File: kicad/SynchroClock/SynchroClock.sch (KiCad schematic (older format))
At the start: 13 parts

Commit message: using atmega328 for now
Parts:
- removed IC?: ATTINY85-P, DIP8, symbol ATTINY85-P
- added D? (x2): 1N4001, pth-semi:DO-41, symbol 1N4001
- added P?: CONN_01X02, symbol CONN_01X02
- added U?: ATMEGA328-PU, dip-sip:DIP-28, symbol ATMEGA328-PU
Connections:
- net labels removed: A, B, CLOCK_A, CLOCK_B, SCL, SDA, SQW
- wire segments 34 -> 46
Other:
- moved on the sheet: D?, U?
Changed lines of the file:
@@
-$EndComp
-$Comp
-L ATTINY85-P IC?
-U 1 1 58C75634
-P 8200 3450
-F 0 "IC?" H 7050 3850 50  0000 C CNN
-F 1 "ATTINY85-P" H 9200 3050 50  0000 C CNN
-F 2 "DIP8" H 9200 3450 50  0000 C CIN
-F 3 "" H 8200 3450 50  0000 C CNN
-	1    8200 3450
-	1    0    0    -1
 $EndComp
 $Comp
 L DS3231 U?
 U 1 1 58C756EE
-P 5400 3400
-F 0 "U?" H 5300 3875 50  0000 R CNN
-F 1 "DS3231" H 5300 3800 50  0000 R CNN
-F 2 "Housings_SOIC:SOIC-16_7.5x10.3mm_Pitch1.27mm" H 5450 3000 50  0001 L CNN
-F 3 "" H 5670 3650 50  0001 C CNN
-	1    5400 3400
-	1    0    0    -1
-$EndComp
-Text Label 4700 3300 0    60   ~ 0
-SCL
-Text Label 3950 3350 2    60   ~ 0
-SCL
-Text Label 3950 3450 2    60   ~ 0
-SDA
-Text Label 4700 3400 0    60   ~ 0
-SDA
-Text Label 6650 3400 0    60   ~ 0
-SCL
-Text Label 6650 3200 0    60   ~ 0
-SDA
-Wire Wire Line
-	4900 3300 4700 3300
-Wire Wire Line
-	4900 3400 4700 3400
-Wire Wire Line
-	3750 3350 3950 3350
-Wire Wire Line
-	3750 3450 3950 3450
-Wire Wire Line
-	6850 3200 6650 3200
-Wire Wire Line
-	6850 3400 6650 3400
+P 4250 2400
+F 0 "U?" H 4150 2875 50  0000 R CNN
+F 1 "DS3231" H 4150 2800 50  0000 R CNN
+F 2 "Housings_SOIC:SOIC-16_7.5x10.3mm_Pitch1.27mm" H 4300 2000 50  0001 L CNN
+F 3 "" H 4520 2650 50  0001 C CNN
+	1    4250 2400
+	0    -1   -1   0
+$EndComp
 $Comp
 L 2N3904 Q?
@@
 Connection ~ 2300 5900
 Wire Wire Line
-	2300 5900 3250 5900
-Wire Wire Line
 	4750 5200 4750 5500
 Wire Wire Line
@@
 	1500 6200 1700 6200
 Connection ~ 1500 5900
-Text Label 5600 5900 0    60   ~ 0
-A
-Text Label 1400 5900 2    60   ~ 0
-B
-Wire Wire Line
-	5600 5900 5500 5900
-Wire Wire Line
-	1400 5900 1500 5900
-Wire Wire Line
-	3650 5900 4750 5900
 $Comp
 L +3.3 #PWR?
@@
 L 1N4001 D?
 U 1 1 58D095EF
-P 3450 6050
-F 0 "D?" V 3600 6050 50  0000 C CNN
-F 1 "1N4001" V 3700 6000 50  0000 C CNN
-F 2 "pth-semi:DO-41" H 3450 5900 50  0001 C CNN
-F 3 "" H 3450 6050 60  0000 C CNN
-F 4 "DIODE 1N4001" H 3450 5800 60  0001 C CNN "BOM"
-	1    3450 6050
+P 3800 6050
+F 0 "D?" V 3950 6050 50  0000 C CNN
+F 1 "1N4001" V 4050 6000 50  0000 C CNN
+F 2 "pth-semi:DO-41" H 3800 5900 50  0001 C CNN
+F 3 "" H 3800 6050 60  0000 C CNN
+F 4 "DIODE 1N4001" H 3800 5800 60  0001 C CNN "BOM"
+	1    3800 6050
 	0    -1   1    0
 $EndComp
@@
 L 1N4001 D?
 U 1 1 58D0972D
-P 3450 5750
-F 0 "D?" V 3600 5750 50  0000 C CNN
-F 1 "1N4001" V 3700 5700 50  0000 C CNN
-F 2 "pth-semi:DO-41" H 3450 5600 50  0001 C CNN
-F 3 "" H 3450 5750 60  0000 C CNN
-F 4 "DIODE 1N4001" H 3450 5500 60  0001 C CNN "BOM"
-	1    3450 5750
+P 3800 5750
+F 0 "D?" V 3950 5750 50  0000 C CNN
+F 1 "1N4001" V 4050 5700 50  0000 C CNN
+F 2 "pth-semi:DO-41" H 3800 5600 50  0001 C CNN
+F 3 "" H 3800 5750 60  0000 C CNN
+F 4 "DIODE 1N4001" H 3800 5500 60  0001 C CNN "BOM"
+	1    3800 5750
 	0    1    -1   0
 $EndComp
-Wire Wire Line
-	3350 5750 3250 5750
-Wire Wire Line
-	3250 5750 3250 6450
-Wire Wire Line
-	3250 6050 3350 6050
-Wire Wire Line
-	3550 5750 3650 5750
-Wire Wire Line
-	3650 5750 3650 6450
-Wire Wire Line
-	3650 6050 3550 6050
-Connection ~ 3650 5900
-Connection ~ 3250 5900
-Connection ~ 3250 6050
-Connection ~ 3650 6050
-Text Label 3250 6450 3    60   ~ 0
-CLOCK_B
-Text Label 3650 6450 3    60   ~ 0
-CLOCK_A
-Text Label 6100 3300 2    60   ~ 0
-SQW
-Wire Wire Line
-	5900 3300 6100 3300
-Text Label 1700 3550 0    60   ~ 0
-SQW
-Wire Wire Line
-	1950 3550 1700 3550
+$Comp
+L 1N4001 D?
+U 1 1 58D3369C
+P 2950 5750
+F 0 "D?" V 3100 5750 50  0000 C CNN
+F 1 "1N4001" V 3200 5700 50  0000 C CNN
+F 2 "pth-semi:DO-41" H 2950 5600 50  0001 C CNN
+F 3 "" H 2950 5750 60  0000 C CNN
+F 4 "DIODE 1N4001" H 2950 5500 60  0001 C CNN "BOM"
+	1    2950 5750
+	0    1    -1   0
+$EndComp
+$Comp
+L 1N4001 D?
+U 1 1 58D336DD
+P 2950 6050
+F 0 "D?" V 3100 6050 50  0000 C CNN
+F 1 "1N4001" V 3200 6000 50  0000 C CNN
+F 2 "pth-semi:DO-41" H 2950 5900 50  0001 C CNN
+F 3 "" H 2950 6050 60  0000 C CNN
+F 4 "DIODE 1N4001" H 2950 5800 60  0001 C CNN "BOM"
+	1    2950 6050
+	0    -1   1    0
+$EndComp
+Wire Wire Line
+	2850 5750 2850 6050
+Wire Wire Line
+	3050 5750 3050 6050
+Wire Wire Line
+	3700 5750 3700 6050
+Wire Wire Line
+	3900 5750 3900 6050
+Connection ~ 3900 5900
+Connection ~ 3700 5900
+Connection ~ 3050 5900
+Connection ~ 2850 5900
+Wire Wire Line
+	4750 5900 3900 5900
+Wire Wire Line
+	2850 5900 2300 5900
+$Comp
+L CONN_01X02 P?
+U 1 1 58D33A1E
+P 3350 6750
+F 0 "P?" H 3350 6900 50  0000 C CNN
+F 1 "CONN_01X02" V 3450 6750 50  0001 C CNN
+F 2 "" H 3350 6750 50  0000 C CNN
+F 3 "" H 3350 6750 50  0000 C CNN
+	1    3350 6750
+	0    1    1    0
+$EndComp
+Wire Wire Line
+	3050 5900 3300 5900
+Wire Wire Line
+	3300 5900 3300 6550
+Wire Wire Line
+	3400 6550 3400 5900
+Wire Wire Line
+	3400 5900 3700 5900
+$Comp
+L ATMEGA328-PU U?
+U 1 1 58D33C8A
+P 7500 3450
+F 0 "U?" H 7500 5000 50  0000 C CNN
+F 1 "ATMEGA328-PU" H 7500 4900 50  0000 C CNN
+F 2 "dip-sip:DIP-28" H 7500 2150 50  0001 C CNN
+F 3 "http://www.atmel.com/images/Atmel-8271-8-bit-AVR-Microcontroller-ATmega48A-48PA-88A-88PA-168A-168PA-328-328P_datasheet_Complete.pdf" H 7500 2050 50  0001 C CNN
+F 4 "ATMEGA328-PU" H 7500 1750 50  0001 C CNN "MPN"
+F 5 "Microchip" H 7500 1850 50  0001 C CNN "Manuf"
+F 6 "Microchip ATMEGA328-PU" H 7500 1950 50  0001 C CNN "BOM"
+	1    7500 3450
+	-1   0    0    -1
+$EndComp
+Wire Wire Line
+	3750 3350 4150 3350
+Wire Wire Line
+	4150 2900 4150 3550
+Wire Wire Line
+	4250 2900 4250 3450
+Wire Wire Line
+	3750 3450 6650 3450
+Connection ~ 4250 3450
+Wire Wire Line
+	4150 3550 6650 3550
+Connection ~ 4150 3350
+Wire Wire Line
+	4150 1900 1800 1900
+Wire Wire Line
+	1800 1900 1800 3550
+Wire Wire Line
+	1800 3550 1950 3550
+Wire Wire Line
+	6650 4350 6100 4350
+Wire Wire Line
+	6100 4350 6100 5900
+Wire Wire Line
+	6100 5900 5500 5900
+Wire Wire Line
+	6650 4250 6000 4250
+Wire Wire Line
+	6000 4250 6000 4900
+Wire Wire Line
+	6000 4900 1300 4900
+Wire Wire Line
+	1300 4900 1300 5900
+Wire Wire Line
+	1300 5900 1500 5900
+Wire Wire Line
+	4150 1900 4150 1700
+Wire Wire Line
+	4150 1700 6300 1700
+Wire Wire Line
+	6300 1700 6300 4150
+Wire Wire Line
+	6300 4150 6650 4150
 $EndSCHEMATC

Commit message: update schematic (WIP)
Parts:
- removed D? (x4): 1N4001, pth-semi:DO-41, symbol 1N4001
- removed P?: CONN_01X02, symbol CONN_01X02
- removed Q? (x2): 2N3904, pth-semi:TO-92, symbol 2N3904
- removed Q? (x2): 2N3906, pth-semi:TO-92, symbol 2N3906
- removed R? (x4): 2.2k, symbol R
- added U?: DRV8838, symbol DRV8838
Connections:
- net labels added: 1HZ, ENABLE, PHASE, SCL, SDA
- wire segments 46 -> 33
- no-connect marks 0 -> 29
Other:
- moved on the sheet: U?

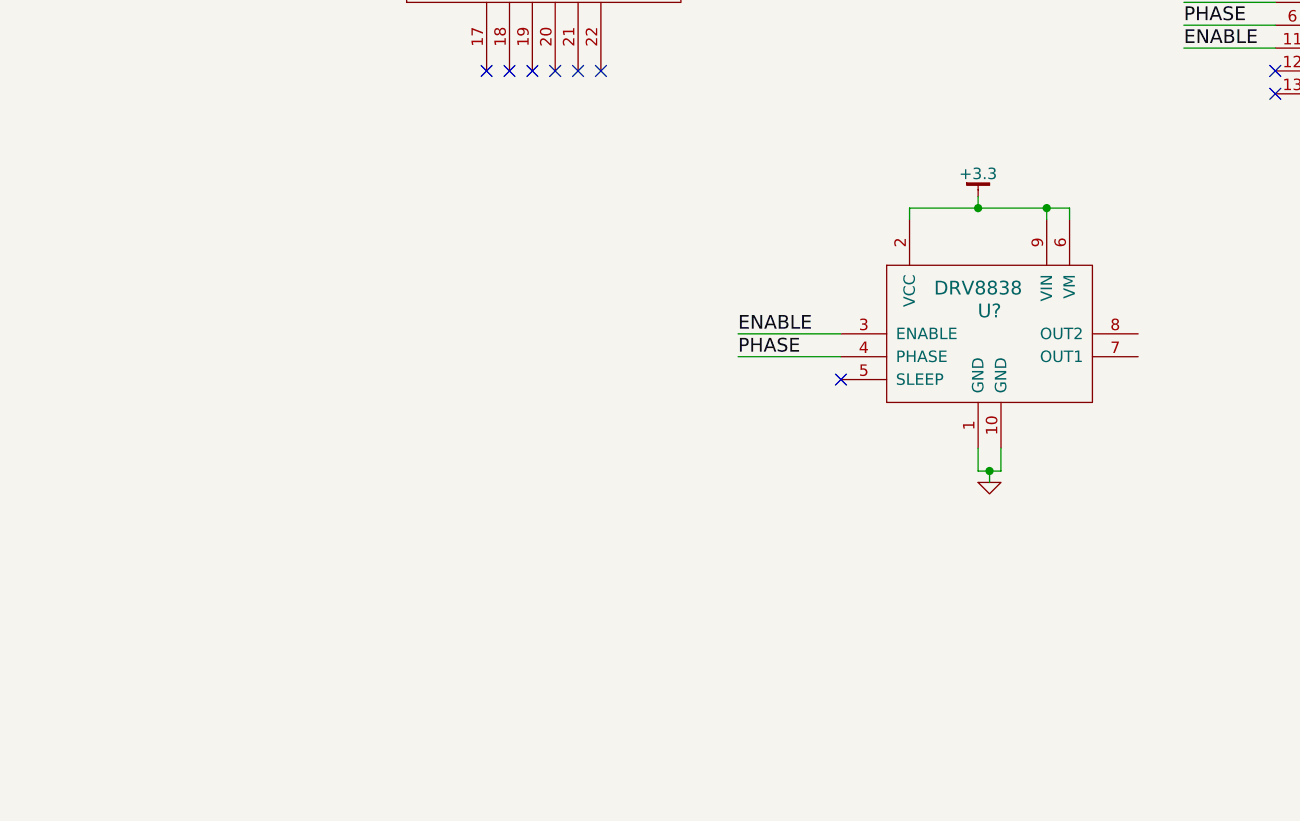
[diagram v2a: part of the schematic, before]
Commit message: added diodes to drop clock output voltage
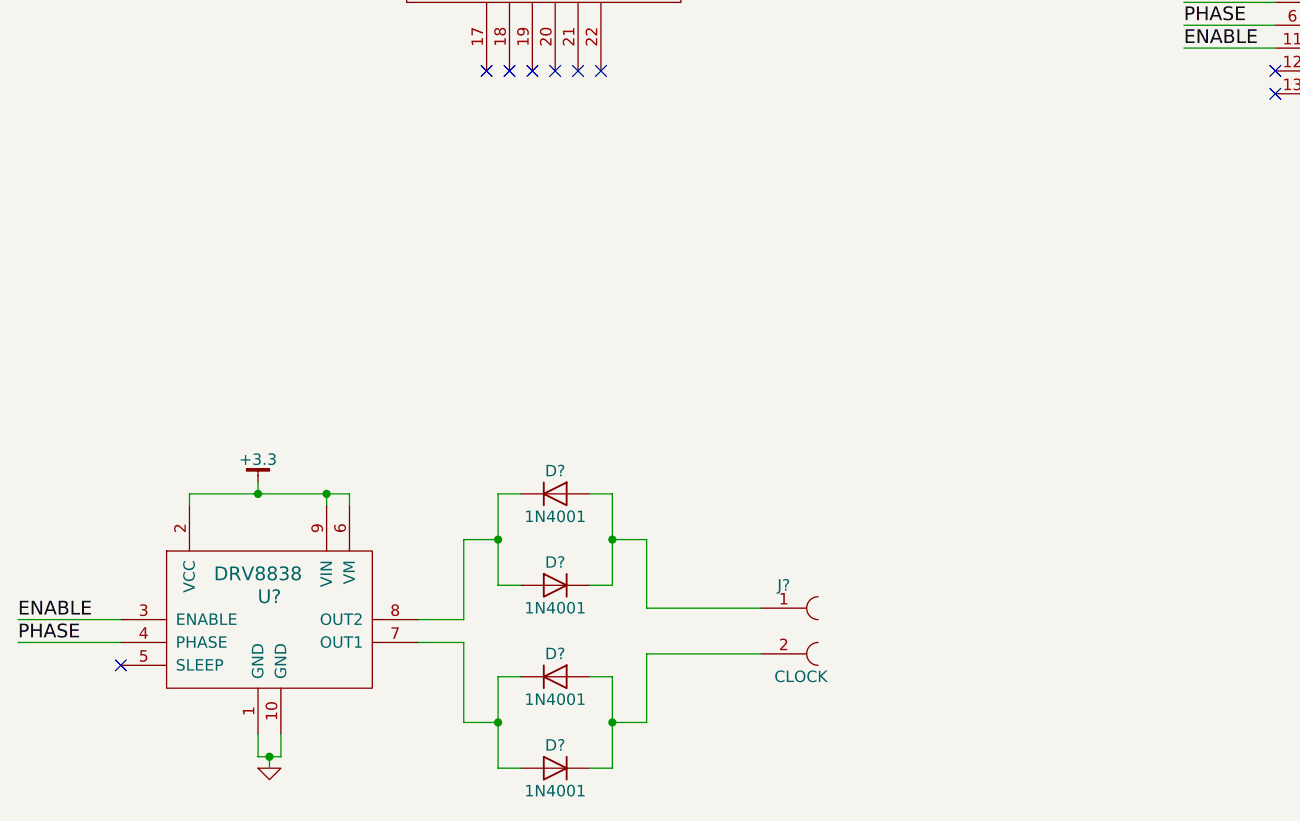
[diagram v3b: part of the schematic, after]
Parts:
- added D? (x4): 1N4001, Diodes_THT:D_DO-41_SOD81_Horizontal_RM10, symbol 1N4001
- added J?: CLOCK, symbol CONN_01X02_FEMALE
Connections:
- net at U?.7 (OUT1): now also D?.1 (K), D?.2 (A)
- net at U?.8 (OUT2): now also D?.1 (K), D?.2 (A)
- new net: D?.1 (K), D?.2 (A), J?.1
- new net: D?.1 (K), D?.2 (A), J?.2
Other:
- moved on the sheet: U?
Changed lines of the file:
@@
 Wire Wire Line
 	4800 3550 5100 3550
-Text Label 4750 5700 0    60   ~ 0
+Text Label 1600 6950 0    60   ~ 0
 ENABLE
-Text Label 4750 5800 0    60   ~ 0
+Text Label 1600 7050 0    60   ~ 0
 PHASE
 Wire Wire Line
-	4750 5700 5200 5700
+	1600 6950 2050 6950
 Wire Wire Line
-	4750 5800 5200 5800
+	1600 7050 2050 7050
 $Comp
 L DRV8838 U?
 U 1 1 58D7D0C2
-P 5850 5400
-F 0 "U?" H 5850 5200 60  0000 C CNN
-F 1 "DRV8838" H 5800 5300 60  0000 C CNN
-F 2 "" H 5850 5400 60  0001 C CNN
-F 3 "" H 5850 5400 60  0001 C CNN
-	1    5850 5400
+P 2700 6650
+F 0 "U?" H 2700 6450 60  0000 C CNN
+F 1 "DRV8838" H 2650 6550 60  0000 C CNN
+F 2 "" H 2700 6650 60  0001 C CNN
+F 3 "" H 2700 6650 60  0001 C CNN
+	1    2700 6650
 	1    0    0    -1
 $EndComp
-NoConn ~ 5200 5900
+NoConn ~ 2050 7150
 $Comp
 L GND #PWR?
 U 1 1 58D7D0FF
-P 5850 6350
-F 0 "#PWR?" H 5850 6350 30  0001 C CNN
-F 1 "GND" H 5850 6280 30  0001 C CNN
-F 2 "" H 5850 6350 60  0000 C CNN
-F 3 "" H 5850 6350 60  0000 C CNN
-	1    5850 6350
+P 2700 7600
+F 0 "#PWR?" H 2700 7600 30  0001 C CNN
+F 1 "GND" H 2700 7530 30  0001 C CNN
+F 2 "" H 2700 7600 60  0000 C CNN
+F 3 "" H 2700 7600 60  0000 C CNN
+	1    2700 7600
 	1    0    0    -1
 $EndComp
 Wire Wire Line
-	5850 6350 5850 6300
+	2700 7600 2700 7550
 Wire Wire Line
-	5800 6300 5900 6300
+	2650 7550 2750 7550
 Wire Wire Line
-	5900 6300 5900 6200
+	2750 7550 2750 7450
 Wire Wire Line
-	5800 6200 5800 6300
-Connection ~ 5850 6300
+	2650 7450 2650 7550
+Connection ~ 2700 7550
 $Comp
 L +3.3 #PWR?
 U 1 1 58D7D184
-P 5800 5100
-F 0 "#PWR?" H 5800 5150 30  0001 C CNN
-F 1 "+3.3" H 5800 5200 50  0000 C CNN
-F 2 "" H 5800 5100 60  0000 C CNN
-F 3 "" H 5800 5100 60  0000 C CNN
-	1    5800 5100
+P 2650 6350
+F 0 "#PWR?" H 2650 6400 30  0001 C CNN
+F 1 "+3.3" H 2650 6450 50  0000 C CNN
+F 2 "" H 2650 6350 60  0000 C CNN
+F 3 "" H 2650 6350 60  0000 C CNN
+	1    2650 6350
 	1    0    0    -1
 $EndComp
 Wire Wire Line
-	5800 5100 5800 5150
+	2650 6350 2650 6400
 Wire Wire Line
-	5500 5200 5500 5150
+	2350 6450 2350 6400
 Wire Wire Line
-	5500 5150 6200 5150
+	2350 6400 3050 6400
 Wire Wire Line
-	6100 5150 6100 5200
+	2950 6400 2950 6450
 Wire Wire Line
-	6200 5150 6200 5200
-Connection ~ 5800 5150
-Connection ~ 6100 5150
+	3050 6400 3050 6450
+Connection ~ 2650 6400
+Connection ~ 2950 6400
+$Comp
+L 1N4001 D?
+U 1 1 58D7DA00
+P 3950 6400
+F 0 "D?" H 3950 6500 50  0000 C CNN
+F 1 "1N4001" H 3950 6300 50  0000 C CNN
+F 2 "Diodes_THT:D_DO-41_SOD81_Horizontal_RM10" H 3950 6225 50  0001 C CNN
+F 3 "" H 3950 6400 50  0001 C CNN
+	1    3950 6400
+	1    0    0    -1
+$EndComp
+$Comp
+L 1N4001 D?
+U 1 1 58D7DA54
+P 3950 6800
+F 0 "D?" H 3950 6900 50  0000 C CNN
+F 1 "1N4001" H 3950 6700 50  0000 C CNN
+F 2 "Diodes_THT:D_DO-41_SOD81_Horizontal_RM10" H 3950 6625 50  0001 C CNN
+F 3 "" H 3950 6800 50  0001 C CNN
+	1    3950 6800
+	-1   0    0    -1
+$EndComp
+$Comp
+L 1N4001 D?
+U 1 1 58D7DA9D
+P 3950 7200
+F 0 "D?" H 3950 7300 50  0000 C CNN
+F 1 "1N4001" H 3950 7100 50  0000 C CNN
+F 2 "Diodes_THT:D_DO-41_SOD81_Horizontal_RM10" H 3950 7025 50  0001 C CNN
+F 3 "" H 3950 7200 50  0001 C CNN
+	1    3950 7200
+	1    0    0    -1
+$EndComp
+$Comp
+L 1N4001 D?
+U 1 1 58D7DACD
+P 3950 7600
+F 0 "D?" H 3950 7700 50  0000 C CNN
+F 1 "1N4001" H 3950 7500 50  0000 C CNN
+F 2 "Diodes_THT:D_DO-41_SOD81_Horizontal_RM10" H 3950 7425 50  0001 C CNN
+F 3 "" H 3950 7600 50  0001 C CNN
+	1    3950 7600
+	-1   0    0    -1
+$EndComp
+Wire Wire Line
+	4100 7200 4200 7200
+Wire Wire Line
+	4200 7200 4200 7600
+Wire Wire Line
+	4200 7600 4100 7600
+Wire Wire Line
+	3800 7200 3700 7200
+Wire Wire Line
+	3700 7200 3700 7600
+Wire Wire Line
+	3700 7600 3800 7600
+Wire Wire Line
+	3350 7050 3550 7050
+Wire Wire Line
+	3550 7050 3550 7400
+Wire Wire Line
+	3550 7400 3700 7400
+Connection ~ 3700 7400
+$Comp
+L CONN_01X02_FEMALE J?
+U 1 1 58D7DDE0
+P 4950 7000
+F 0 "J?" H 4950 7200 50  0000 C CNN
+F 1 "CLOCK" H 5025 6800 50  0000 C CNN
+F 2 "" H 4950 7100 50  0001 C CNN
+F 3 "" H 4950 7100 50  0001 C CNN
+	1    4950 7000
+	1    0    0    -1
+$EndComp
+Wire Wire Line
+	3800 6400 3700 6400
+Wire Wire Line
+	3700 6400 3700 6800
+Wire Wire Line
+	3700 6800 3800 6800
+Wire Wire Line
+	3350 6950 3550 6950
+Wire Wire Line
+	3550 6950 3550 6600
+Wire Wire Line
+	3550 6600 3700 6600
+Connection ~ 3700 6600
+Wire Wire Line
+	4100 6400 4200 6400
+Wire Wire Line
+	4200 6400 4200 6800
+Wire Wire Line
+	4200 6800 4100 6800
+Wire Wire Line
+	4850 6900 4350 6900
+Wire Wire Line
+	4350 6900 4350 6600
+Wire Wire Line
+	4350 6600 4200 6600
+Connection ~ 4200 6600
+Wire Wire Line
+	4850 7100 4350 7100
+Wire Wire Line
+	4350 7100 4350 7400
+Wire Wire Line
+	4350 7400 4200 7400
+Connection ~ 4200 7400
 $EndSCHEMATC

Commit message: more schematic work
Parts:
- added D1: LED, LEDs:LED_D3.0mm, symbol LED
- added R1, R2, R3, R7, R8, R9: 10k, Resistors_THT:R_Axial_DIN0204_L3.6mm_D1.6mm_P1.90mm_Vertical, symbol R
- added R4, R5: 1k, Resistors_THT:R_Axial_DIN0204_L3.6mm_D1.6mm_P1.90mm_Vertical, symbol R
- added R6: 220, Resistors_THT:R_Axial_DIN0204_L3.6mm_D1.6mm_P1.90mm_Vertical, symbol R
- added SW1: FactoryReset, Buttons_Switches_THT:SW_PUSH_6mm, symbol SW_Push
- D2, D3, D4, D5: renamed from D?; footprint Diodes_THT:D_DO-41_SOD81_Horizontal_RM10 -> Diodes_THT:D_DO-41_SOD81_P2.54mm_Vertical_AnodeUp
- J1: renamed from J?; footprint (none) -> Connectors:PINHEAD1-2
- U2: renamed from U?; footprint (none) -> ESP8266:ESP-12E
- gave numbers to parts that had none: 3
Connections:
- net +3.3: now also D1.2 (A), R1.1, R2.1, R3.1, R8.2, R9.2
- net GND: now also R7.2, SW1.1
- net SCL: now also U3.16 (SCL)
- net SDA: now also U3.15 (SDA)
- net at U2.1 (REST): now also R3.2
- net at U2.10 (GPIO15): now also R7.1
- net at U2.11 (GPIO2): now also R8.1
- net GPIO0: now reaches U2.12 (GPIO0)
- net GPIO0: now also R9.1
- net RX: now reaches U2.15 (RXD)
- net TX: now reaches U2.16 (TXD)
- net at U2.3 (CH_PD): now also R4.1
- net at U2.6 (GPIO12): now also R5.1
- net at U2.7 (GPIO13): now also R6.2
- new net: R1.2, R5.2, SW1.2
- new net: D1.1 (K), R6.1
- new net RESET: R2.2, R4.2
